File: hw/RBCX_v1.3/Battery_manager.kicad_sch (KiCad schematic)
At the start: 74 parts, among them Q10 Q_PMOS_DGS, Q11 Q_PMOS_DGS, Q12 JSM3622, Q13 2N7002KDW, Q7 Q_NMOS_DGS, Q8 Q_NMOS_DGS, Q9 Q_PMOS_DGS, SW13 SW, SW14 SW, U18 MP2651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

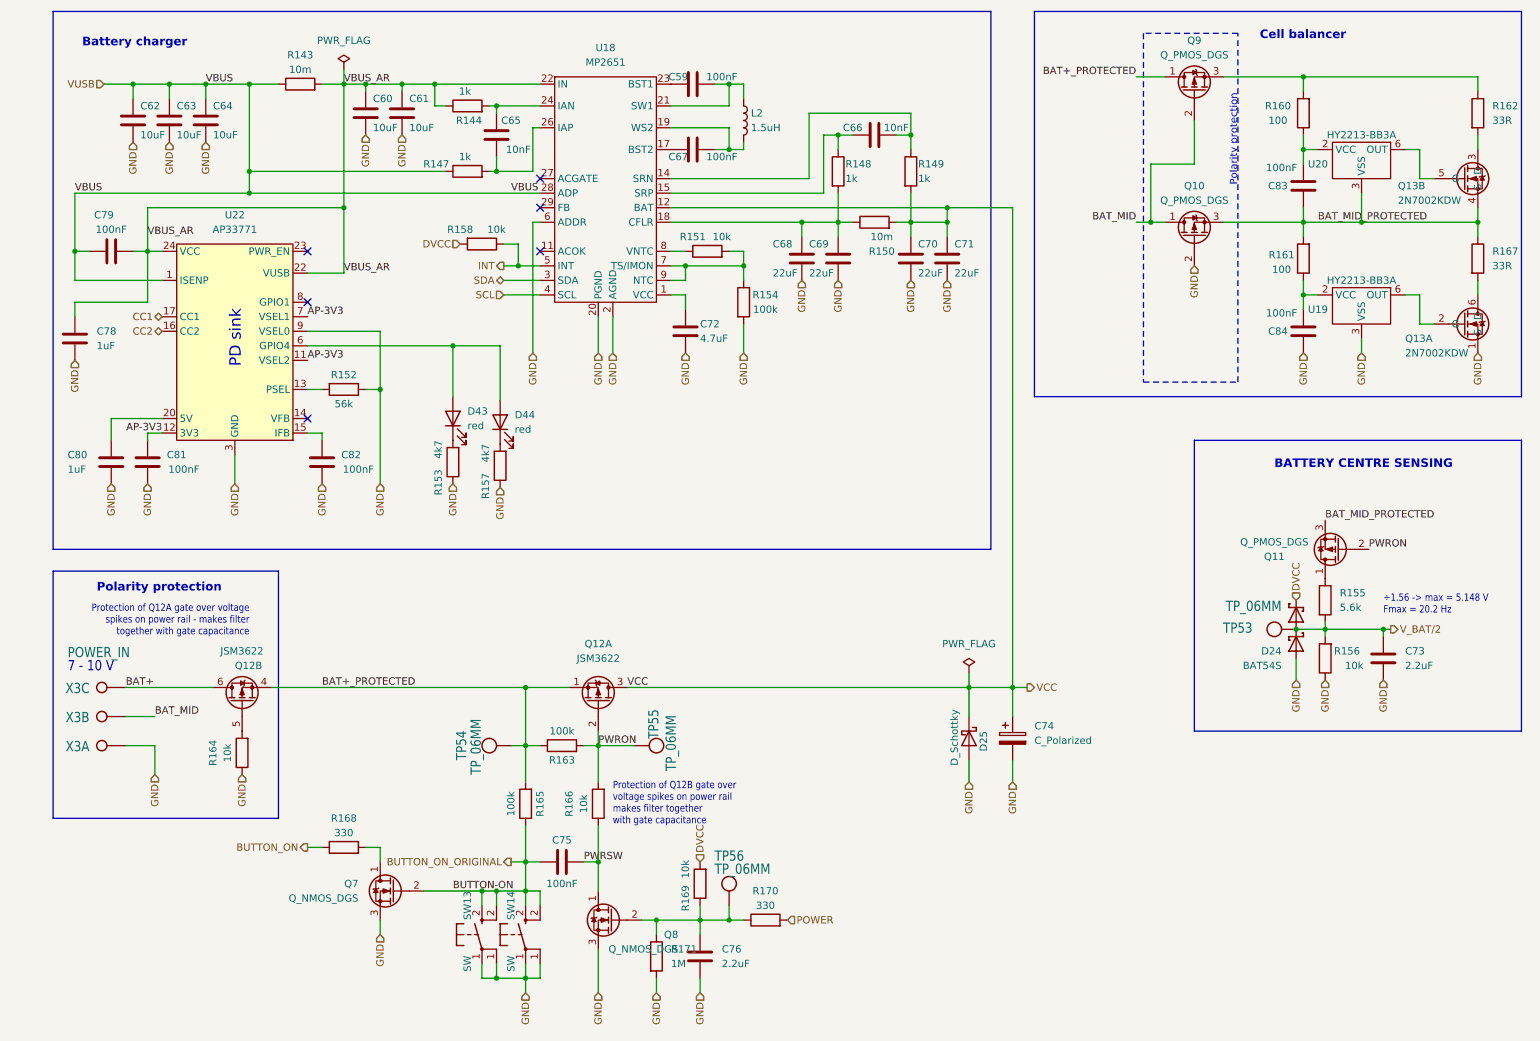
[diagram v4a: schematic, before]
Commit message: Kuba issues
Change of power transistor from JSM3622 to JMSL0302AU

NTC connectors

Moving the Cell balancer behind the switch

and some little things
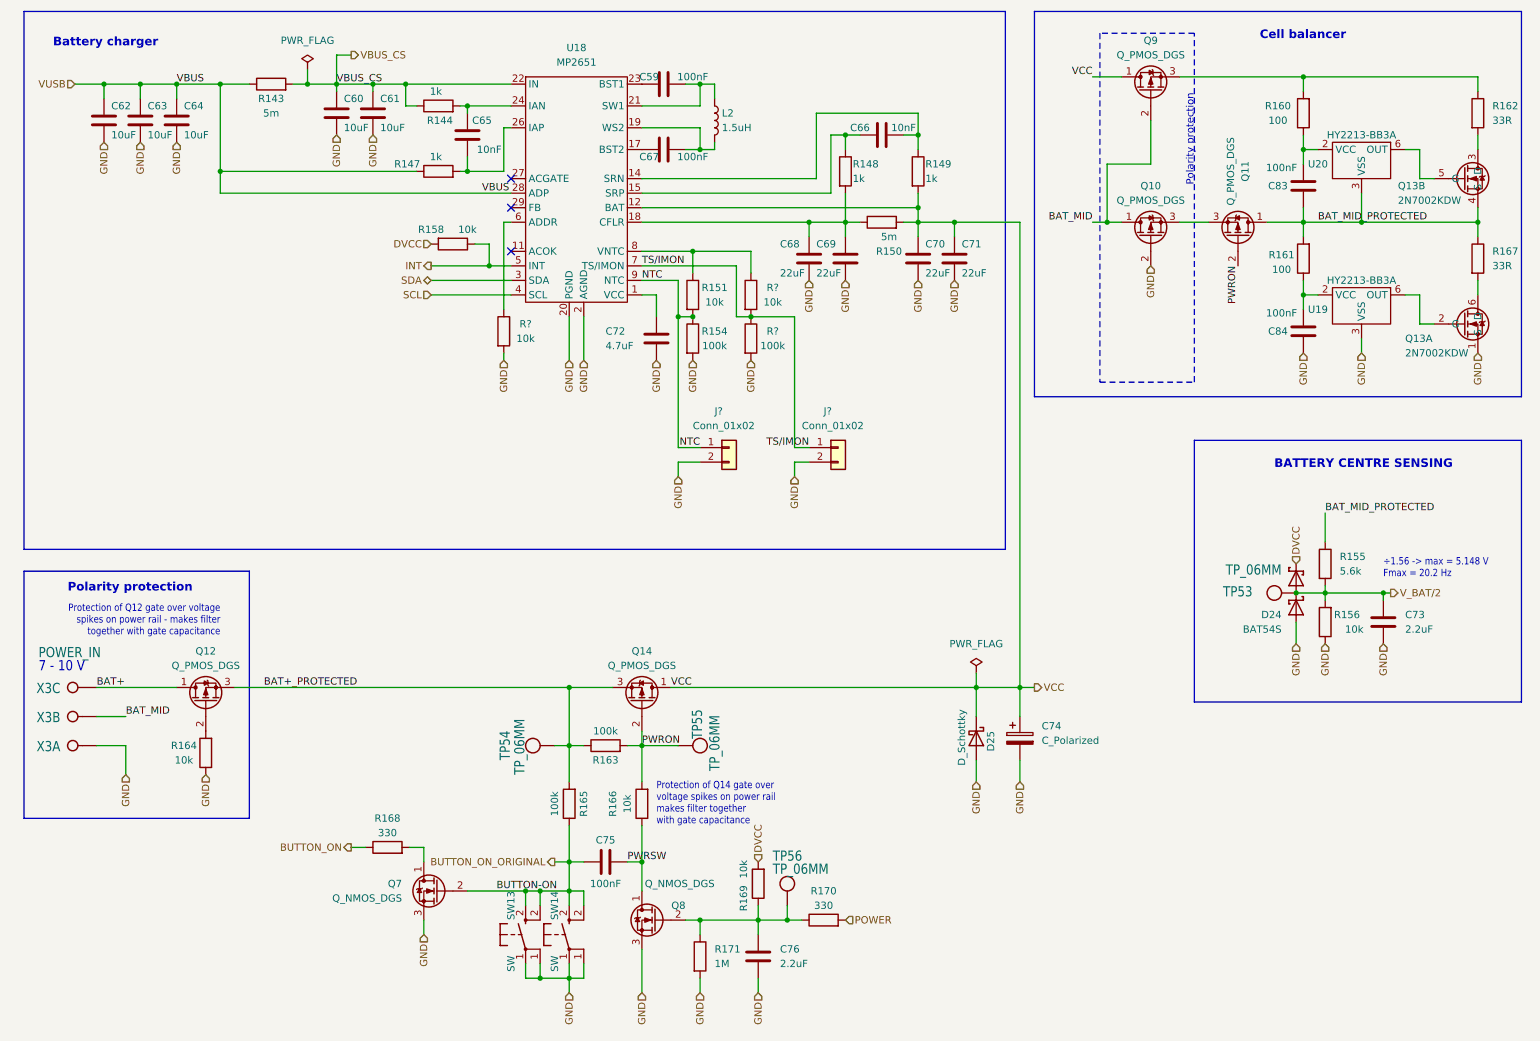
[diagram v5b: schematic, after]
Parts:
- removed C78, C80: 1uF, Resistor_SMD:R_0402_1005Metric, symbol Device:C
- removed C79, C81, C82: 100nF, Capacitor_SMD:C_0402_1005Metric, symbol Device:C
- removed D43, D44: red, LED_SMD:LED_0603_1608Metric, symbol Device:LED
- removed Q12: JSM3622, RBCX:JSM3622, symbol RBCX:JSM3622
- removed R152: 56k, Capacitor_SMD:C_0402_1005Metric, symbol Device:R
- removed R153, R157: 4k7, Resistor_SMD:R_0201_0603Metric, symbol Device:R
- removed U22: AP33771, Package_DFN_QFN:QFN-24-1EP_4x4mm_P0.5mm_EP2.6x2.6mm, symbol RBCX:AP33771
- added J? (x2): Conn_01x02, Connector_PinSocket_2.54mm:PinSocket_1x02_P2.54mm_Vertical, symbol Connector_Generic:Conn_01x02
- added Q12, Q14: Q_PMOS_DGS, RBCX:JMSL0302AU, symbol Device:Q_PMOS_DGS
- added R?: 100k, Capacitor_SMD:C_0201_0603Metric, symbol Device:R
- added R? (x2): 10k, Capacitor_SMD:C_0201_0603Metric, symbol Device:R
- R143, R150: value 10m -> 5m; LCSC C728271 -> C728267
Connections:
- net BAT+: now also Q12.1 (D)
- net BAT+_PROTECTED: now also Q12.3 (S), Q14.3 (S); no longer Q9.1 (D)
- net BAT_MID_PROTECTED: now also Q11.1 (D), R155.1; no longer Q10.3 (S), Q11.3 (S)
- net GND: now also J?.2 (Pin_2), J?.2 (Pin_2), R?.2, R?.2; no longer U18.6 (ADDR)
- net PWRON: now also Q14.2 (G)
- net VCC: now also Q9.1 (D), Q14.1 (D)
- net NTC: now reaches R151.2, R154.1, U18.10 (NTC), U18.9 (NTC)
- net NTC: now also J?.1 (Pin_1); no longer U18.7 (TS/IMON)
- net at R151.1, U18.8 (VNTC): now also R?.1
- net at R164.2: now also Q12.2 (G)
- net VBUS_AR renamed VBUS_CS
- new net: R?.1, U18.6 (ADDR)
- new net: Q10.3 (S), Q11.3 (S)
- new net TS/IMON: J?.1 (Pin_1), R?.1, R?.2, U18.7 (TS/IMON)
- no-connect marks 6 -> 3
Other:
- note added: "Protection of Q12 gate over voltage spikes on power rail - makes filter together with gate capacitance"
- note added: "Protection of Q14 gate over voltage spikes on power rail makes filter together with gate capacitance"
- note removed: "PD sink"
- note removed: "Protection of Q12A gate over voltage spikes on power rail - makes filter together with gate capacitance"
- note removed: "Protection of Q12B gate over voltage spikes on power rail makes filter together with gate capacitance"
- moved on the sheet: C59, C60, C61, C62, C63, C64, C65, C66, C67, C68, C69, C70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

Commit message: Kuba issues - PCB
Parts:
- gave numbers to parts that had none: 5
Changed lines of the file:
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@@
   (symbol (lib_id "Connector_Generic:Conn_01x02") (at 140.97 93.98 0) (unit 1)
     (in_bom yes) (on_board yes)
-    (property "Reference" "J?" (id 0) (at 138.43 87.63 0)
+    (property "Reference" "J51" (id 0) (at 138.43 87.63 0)
       (effects (font (size 1.27 1.27)) (justify left))
     )
@@
   (symbol (lib_id "Device:R") (at 144.78 74.93 0) (unit 1)
     (in_bom yes) (on_board yes)
-    (property "Reference" "R?" (id 0) (at 148.59 73.66 0))
+    (property "Reference" "R157" (id 0) (at 148.59 73.66 0))
     (property "Value" "100k" (id 1) (at 148.59 76.2 0))
     (property "Footprint" "Capacitor_SMD:C_0201_0603Metric" (id 2) (at 143.002 74.93 90)
@@
   (symbol (lib_id "Device:R") (at 101.6 73.66 0) (unit 1)
     (in_bom yes) (on_board yes)
-    (property "Reference" "R?" (id 0) (at 105.41 72.39 0))
+    (property "Reference" "R153" (id 0) (at 105.41 72.39 0))
     (property "Value" "10k" (id 1) (at 105.41 74.93 0))
     (property "Footprint" "Capacitor_SMD:C_0201_0603Metric" (id 2) (at 99.822 73.66 90)
@@
   (symbol (lib_id "Connector_Generic:Conn_01x02") (at 160.02 93.98 0) (unit 1)
     (in_bom yes) (on_board yes)
-    (property "Reference" "J?" (id 0) (at 157.48 87.63 0)
+    (property "Reference" "J52" (id 0) (at 157.48 87.63 0)
       (effects (font (size 1.27 1.27)) (justify left))
     )
@@
   (symbol (lib_id "Device:R") (at 144.78 67.31 0) (unit 1)
     (in_bom yes) (on_board yes)
-    (property "Reference" "R?" (id 0) (at 148.59 66.04 0))
+    (property "Reference" "R152" (id 0) (at 148.59 66.04 0))
     (property "Value" "10k" (id 1) (at 148.59 68.58 0))
     (property "Footprint" "Capacitor_SMD:C_0201_0603Metric" (id 2) (at 143.002 67.31 90)

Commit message: Few small things
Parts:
- J51, J52: footprint Connector_PinSocket_2.54mm:PinSocket_1x02_P2.54mm_Vertical -> RBCX:PinHeader_1x02_P2.54mm_Vertical
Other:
- moved on the sheet: J52
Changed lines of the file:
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@@
     (stroke (width 0) (type default) (color 0 0 0 0))
   )
-  (wire (pts (xy 152.4 96.52) (xy 154.94 96.52))
+  (wire (pts (xy 152.4 96.52) (xy 161.29 96.52))
     (stroke (width 0) (type default) (color 0 0 0 0))
   )
@@
     (stroke (width 0) (type default) (color 0 0 0 0))
   )
-  (wire (pts (xy 154.94 93.98) (xy 152.4 93.98))
+  (wire (pts (xy 161.29 93.98) (xy 152.4 93.98))
     (stroke (width 0) (type default) (color 0 0 0 0))
   )
@@
     (effects (font (size 1.27 1.27)) (justify right bottom))
   )
-  (label "TS{slash}IMON" (at 154.94 93.98 180)
+  (label "TS{slash}IMON" (at 161.29 93.98 180)
     (effects (font (size 1.27 1.27)) (justify right bottom))
   )
@@
       (effects (font (size 1.27 1.27)) (justify left))
     )
-    (property "Footprint" "Connector_PinSocket_2.54mm:PinSocket_1x02_P2.54mm_Vertical" (id 2) (at 140.97 93.98 0)
+    (property "Footprint" "RBCX:PinHeader_1x02_P2.54mm_Vertical" (id 2) (at 140.97 93.98 0)
       (effects (font (size 1.27 1.27)) hide)
     )
@@
     (pin "2")
   )
-  (symbol (lib_id "Connector_Generic:Conn_01x02") (at 160.02 93.98 0) (unit 1)
-    (in_bom yes) (on_board yes)
-    (property "Reference" "J52" (id 0) (at 157.48 87.63 0)
-      (effects (font (size 1.27 1.27)) (justify left))
-    )
-    (property "Value" "Conn_01x02" (id 1) (at 153.67 90.17 0)
-      (effects (font (size 1.27 1.27)) (justify left))
-    )
-    (property "Footprint" "Connector_PinSocket_2.54mm:PinSocket_1x02_P2.54mm_Vertical" (id 2) (at 160.02 93.98 0)
-      (effects (font (size 1.27 1.27)) hide)
-    )
-    (property "Datasheet" "~" (id 3) (at 160.02 93.98 0)
-      (effects (font (size 1.27 1.27)) hide)
-    )
+  (symbol (lib_id "Connector_Generic:Conn_01x02") (at 166.37 93.98 0) (unit 1)
+    (in_bom yes) (on_board yes)
+    (property "Reference" "J52" (id 0) (at 163.83 87.63 0)
+      (effects (font (size 1.27 1.27)) (justify left))
+    )
+    (property "Value" "Conn_01x02" (id 1) (at 160.02 90.17 0)
+      (effects (font (size 1.27 1.27)) (justify left))
+    )
+    (property "Footprint" "RBCX:PinHeader_1x02_P2.54mm_Vertical" (id 2) (at 166.37 93.98 0)
+      (effects (font (size 1.27 1.27)) hide)
+    )
+    (property "Datasheet" "~" (id 3) (at 166.37 93.98 0)
+      (effects (font (size 1.27 1.27)) hide)
+    )

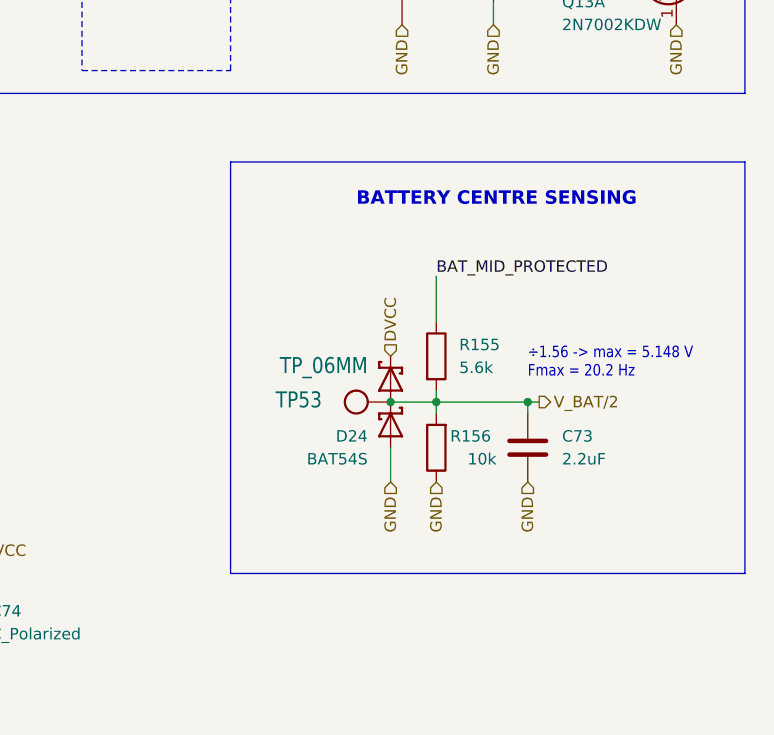
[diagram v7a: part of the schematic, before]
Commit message: USB-DET level shifter
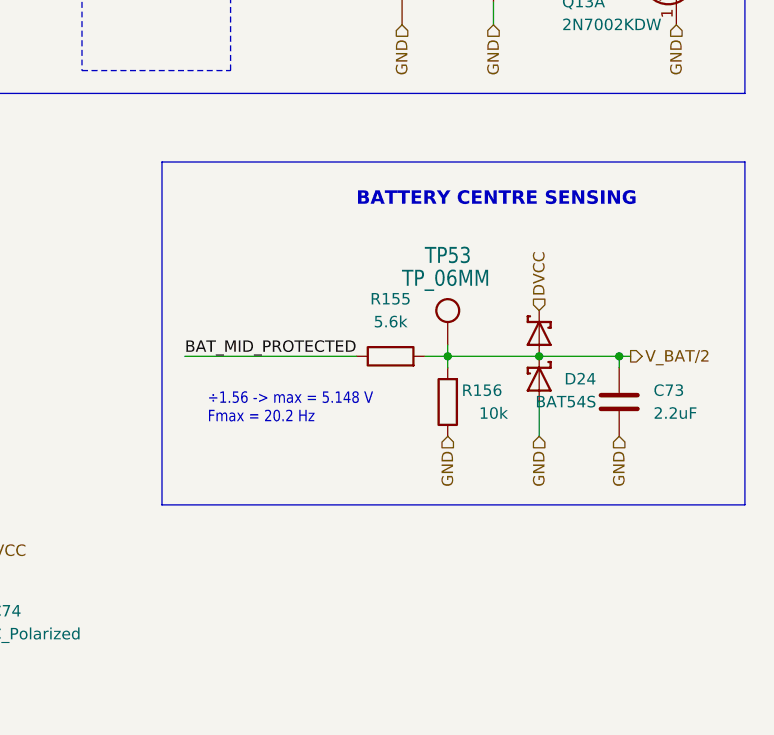
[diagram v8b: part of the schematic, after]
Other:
- moved on the sheet: C73, D24, R155, R156, TP53
